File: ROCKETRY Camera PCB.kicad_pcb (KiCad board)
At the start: 2 copper layers, 111.8 x 67.4 mm, 30 parts, among them J1 Conn_01x02_Pin, J2 Conn_01x03_Pin, J4 Conn_01x01_Pin, J5 Conn_01x01_Pin, U2 AP62200WU

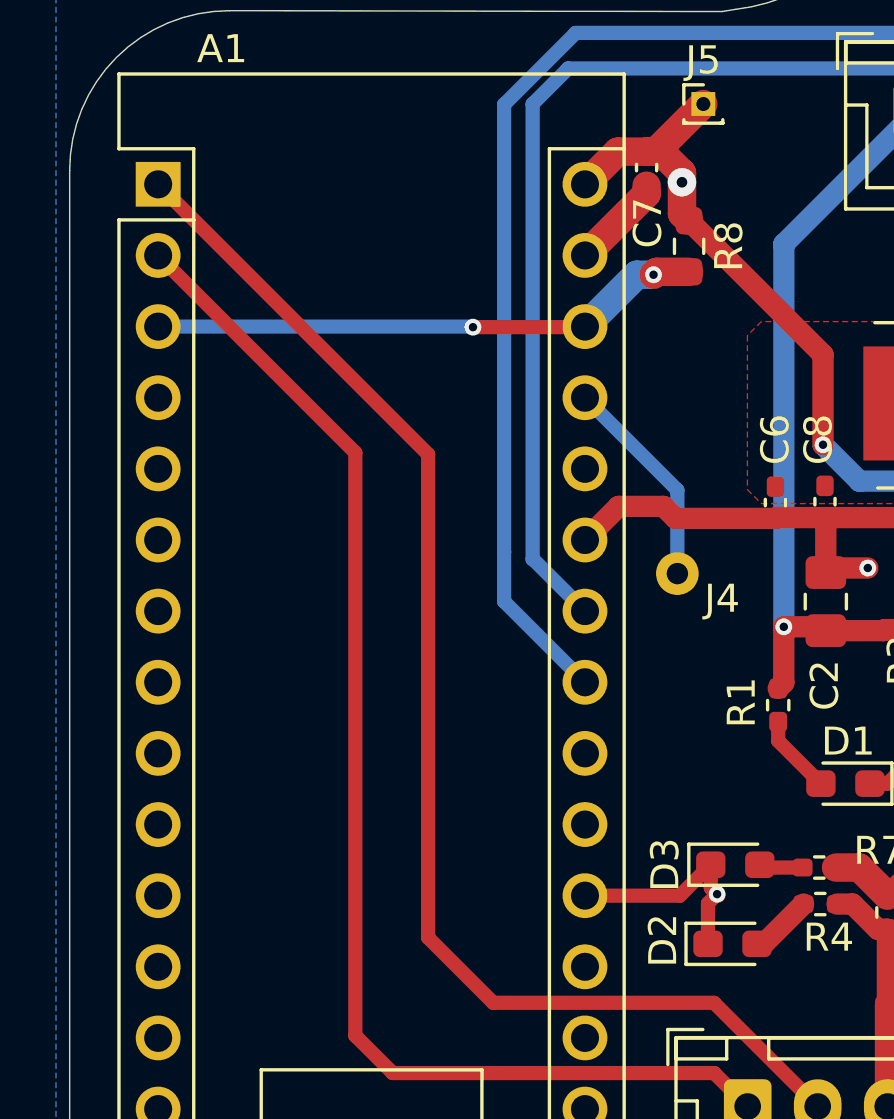
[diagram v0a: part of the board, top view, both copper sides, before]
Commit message: add mounting hole dimension
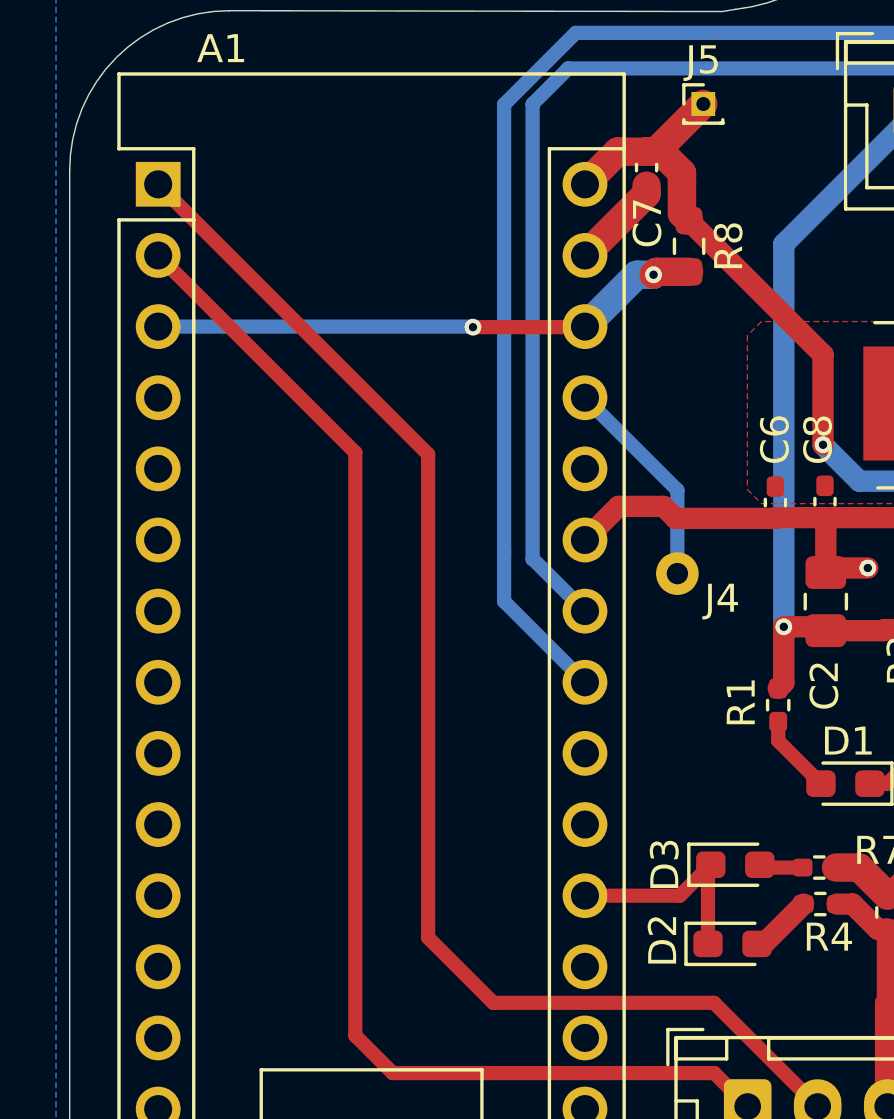
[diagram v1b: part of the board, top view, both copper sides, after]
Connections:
- D2 pad 1: Net-(D2-K) -> GND
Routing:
- net GND: track 37.9 -> 37.6 mm, vias 4 -> 3
- net +5V: vias 3 -> 2
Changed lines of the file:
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@@
 			(sketchpadsonfab no)
 			(subtractmaskfromsilk no)
-			(outputformat 4)
+			(outputformat 1)
 			(mirror no)
 			(drillshape 0)
@@
 	(net 17 "Net-(U2-FB)")
 	(net 18 "Net-(J2-Pin_3)")
-	(net 19 "Net-(D2-K)")
-	(net 20 "unconnected-(U1-3Vo-Pad10)")
-	(net 21 "unconnected-(U2-EN-Pad5)")
-	(net 22 "Net-(A1-+5V)")
+	(net 19 "unconnected-(U1-3Vo-Pad10)")
+	(net 20 "unconnected-(U2-EN-Pad5)")
+	(net 21 "Net-(A1-+5V)")
 	(footprint "Resistor_SMD:R_0603_1608Metric_Pad0.98x0.95mm_HandSolder"
 		(layer "F.Cu")
@@
 			(layers "*.Cu" "*.Mask")
 			(remove_unused_layers no)
-			(net 22 "Net-(A1-+5V)")
+			(net 21 "Net-(A1-+5V)")
 			(pinfunction "+5V")
 			(pintype "power_out")
@@
 			(layers "F.Cu" "F.Paste" "F.Mask")
 			(roundrect_rratio 0.25)
-			(net 19 "Net-(D2-K)")
+			(net 2 "GND")
 			(pinfunction "K")
 			(pintype "passive")
@@
 			(layers "*.Cu" "*.Mask")
 			(remove_unused_layers no)
-			(net 22 "Net-(A1-+5V)")
+			(net 21 "Net-(A1-+5V)")
 			(pinfunction "Pin_1")
 			(pintype "passive")
@@
 			(layers "*.Cu" "F.Mask")
 			(remove_unused_layers no)
-			(net 20 "unconnected-(U1-3Vo-Pad10)")
+			(net 19 "unconnected-(U1-3Vo-Pad10)")
 			(pinfunction "3Vo")
 			(pintype "power_in+no_connect")
@@
 			(layers "F.Cu" "F.Paste" "F.Mask")
 			(roundrect_rratio 0.25)
-			(net 21 "unconnected-(U2-EN-Pad5)")
+			(net 20 "unconnected-(U2-EN-Pad5)")
 			(pinfunction "EN")
 			(pintype "passive+no_connect")
@@
 	)
 	(segment
-		(start 106.593 108.221)
-		(end 106.593 106.771)
-		(width 0.508)
-		(layer "F.Cu")
-		(net 2)
-	)
-	(segment
 		(start 104.4 81.44)
 		(end 104.4 81.1485)
@@
 	)
 	(segment
+		(start 106.593 108.221)
+		(end 106.593 105.496)
+		(width 0.508)
+		(layer "F.Cu")
+		(net 2)
+	)
+	(segment
 		(start 115.51 111.41)
 		(end 115.51 114.029)
@@
 	)
 	(segment
-		(start 106.693 105.396)
-		(end 106.693 106.221)
-		(width 0.508)
-		(layer "F.Cu")
-		(net 2)
-	)
-	(segment
 		(start 110.9625 94.8)
 		(end 110.8 94.9625)
@@
 	)
 	(segment
-		(start 106.693 106.221)
-		(end 106.918 106.446)
-		(width 0.508)
-		(layer "F.Cu")
-		(net 2)
-	)
-	(segment
 		(start 113.82 93.49)
 		(end 113.82 93.42)
@@
 	)
 	(segment
-		(start 106.918 106.446)
-		(end 106.968 106.496)
+		(start 106.593 105.496)
+		(end 106.693 105.396)
 		(width 0.508)
 		(layer "F.Cu")
@@
 	)
 	(segment
-		(start 106.593 106.771)
-		(end 106.918 106.446)
-		(width 0.508)
-		(layer "F.Cu")
-		(net 2)
-	)
-	(segment
 		(start 105.005289 92.6)
 		(end 103.4 92.6)
@@
 	)
 	(via
-		(at 106.918 106.446)
-		(size 0.6)
-		(drill 0.3)
-		(layers "F.Cu" "B.Cu")
-		(net 2)
-	)
-	(via
 		(at 112.3 94.8)
 		(size 0.6)
@@
 	)
 	(segment
-		(start 104.7515 84.2245)
-		(end 104.648 84.328)
-		(width 1.016)
+		(start 102.18 86.2)
+		(end 102.2 86.18)
+		(width 0.508)
 		(layer "F.Cu")
 		(net 4)
 	)
 	(segment
-		(start 105.918 84.2245)
-		(end 104.7515 84.2245)
-		(width 1.016)
+		(start 98.2 86.2)
+		(end 102.18 86.2)
+		(width 0.508)
 		(layer "F.Cu")
 		(net 4)
 	)
 	(segment
-		(start 98.2 86.2)
-		(end 102.18 86.2)
-		(width 0.508)
+		(start 104.648 84.328)
+		(end 104.7515 84.2245)
+		(width 1.016)
 		(layer "F.Cu")
 		(net 4)
 	)
 	(segment
-		(start 102.18 86.2)
-		(end 102.2 86.18)
-		(width 0.508)
+		(start 104.7515 84.2245)
+		(end 105.918 84.2245)
+		(width 1.016)
 		(layer "F.Cu")
 		(net 4)
@@
 	)
 	(segment
-		(start 86.96 86.18)
-		(end 98.18 86.18)
-		(width 0.508)
+		(start 104.648 84.328)
+		(end 104.052 84.328)
+		(width 1.016)
 		(layer "B.Cu")
 		(net 4)
 	)
 	(segment
-		(start 104.052 84.328)
-		(end 102.2 86.18)
-		(width 1.016)
+		(start 98.18 86.18)
+		(end 86.96 86.18)
+		(width 0.508)
 		(layer "B.Cu")
 		(net 4)
 	)
 	(segment
-		(start 104.648 84.328)
-		(end 104.052 84.328)
+		(start 104.052 84.328)
+		(end 102.2 86.18)
 		(width 1.016)
 		(layer "B.Cu")
@@
 	)
 	(segment
-		(start 98.18 86.18)
-		(end 98.2 86.2)
+		(start 98.2 86.2)
+		(end 98.18 86.18)
 		(width 0.508)
 		(layer "B.Cu")
@@
 	)
 	(via
-		(at 105.664 81.026)
-		(size 1.016)
-		(drill 0.381)
-		(layers "F.Cu" "B.Cu")
-		(net 7)
-	)
-	(via
 		(at 110.7 90.4)
 		(size 0.6)
@@
 		(width 0.508)
 		(layer "B.Cu")
-		(net 22)
+		(net 21)
 	)
 	(segment
@@
 		(width 0.508)
 		(layer "B.Cu")
-		(net 22)
+		(net 21)
 	)
 	(zone
